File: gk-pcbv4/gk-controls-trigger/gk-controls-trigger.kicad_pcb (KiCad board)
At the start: 2 copper layers, 60 x 38.2 mm, 7 parts, among them J1 Conn_01x03, J2 Conn_01x01, J3 Conn_01x01, J4 Conn_01x01, J5 Conn_01x01

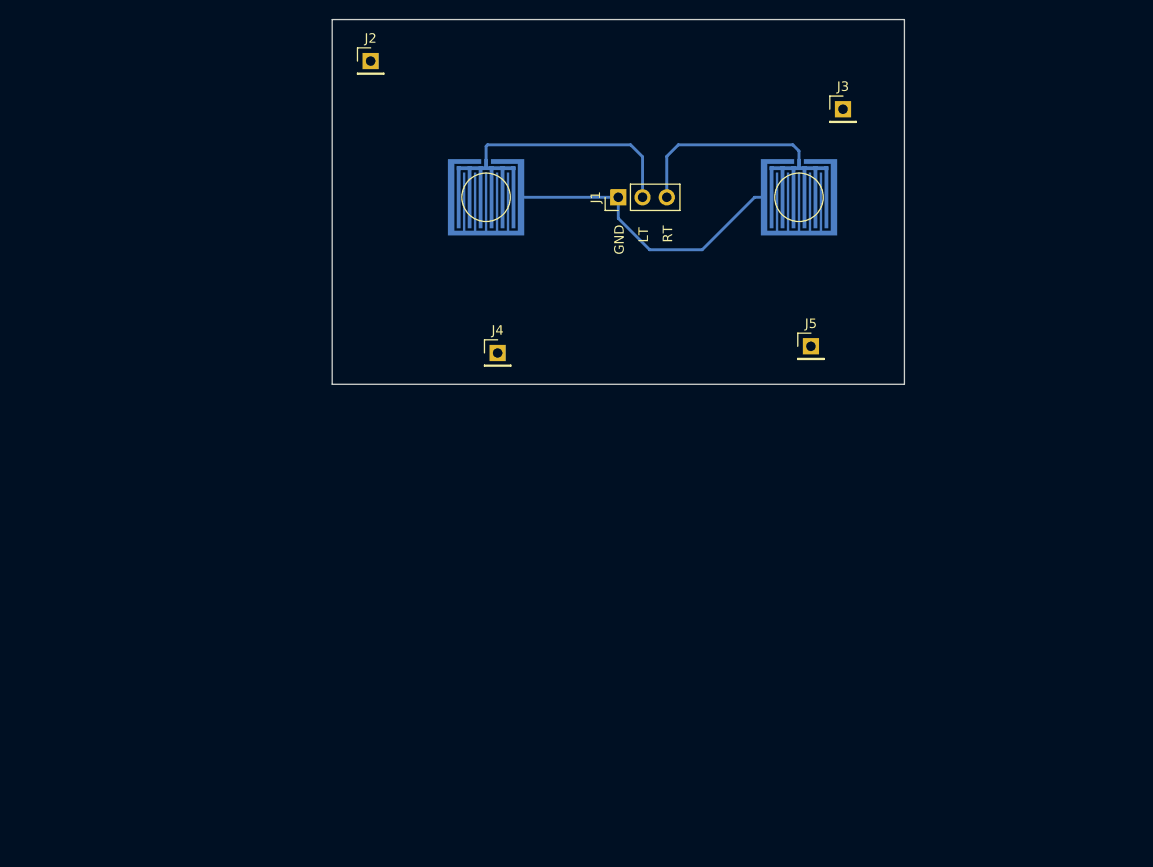
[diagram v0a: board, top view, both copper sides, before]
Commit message: update controls layout triggers now are analog new ADC on control board Move bumper buttons to trigger daughterboard and put in more ergonomical position
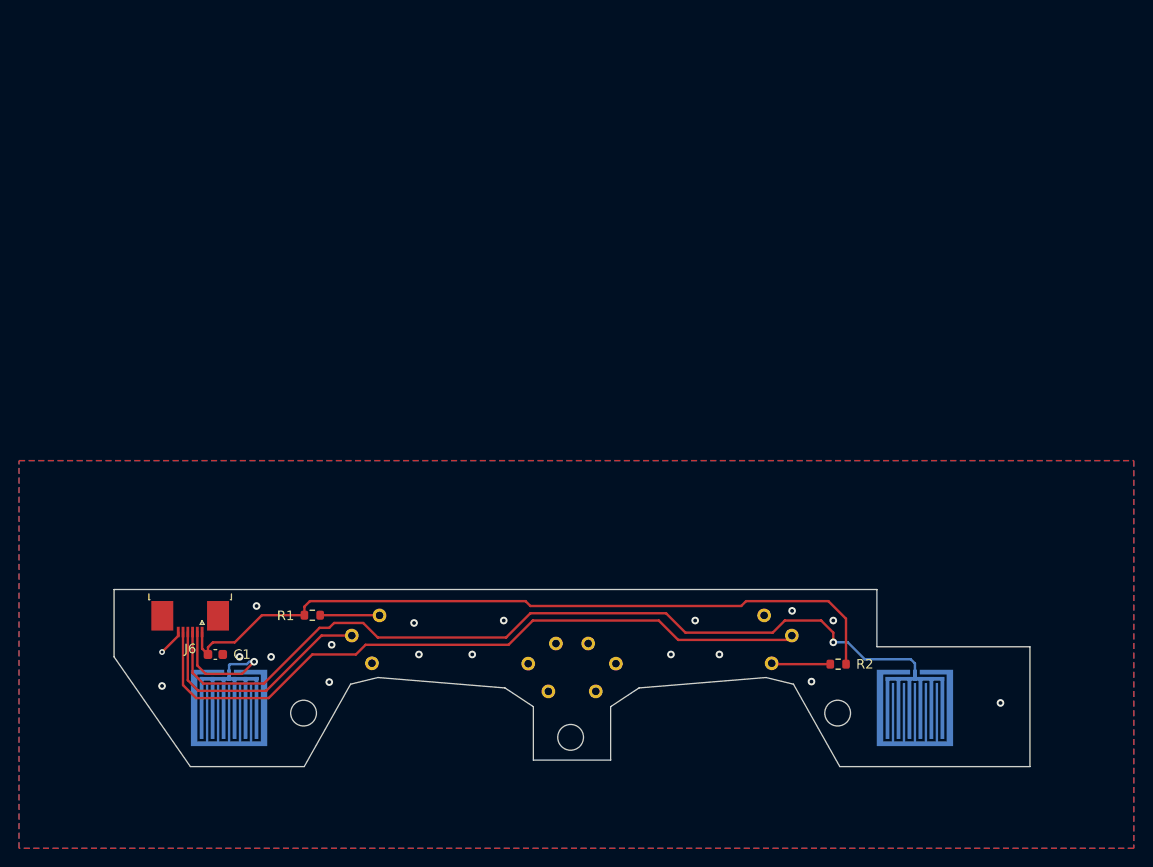
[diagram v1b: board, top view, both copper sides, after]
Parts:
- removed J1: Conn_01x03, Connector_PinHeader_2.54mm:PinHeader_1x03_P2.54mm_Vertical
- removed J2, J3, J4, J5: Conn_01x01, Connector_PinHeader_2.54mm:PinHeader_1x01_P2.54mm_Vertical
- added C1: 1u, Capacitor_SMD:C_0603_1608Metric, F.Cu at (46.0, 121.9)
- added H1: MountingHole, MountingHole:MountingHole_2.7mm_M2.5, F.Cu at (55.2, 128.1)
- added H2: MountingHole, MountingHole:MountingHole_2.7mm_M2.5, F.Cu at (83.2, 130.6)
- added H3: MountingHole, MountingHole:MountingHole_2.7mm_M2.5, F.Cu at (111.2, 128.1)
- added J6: Conn_01x06, Connector_FFC-FPC:TE_0-1734839-6_1x06-1MP_P0.5mm_Horizontal, F.Cu at (43.3, 118.2)
- added R1: 100k/0R, Resistor_SMD:R_0603_1608Metric, F.Cu at (56.1, 117.8)
- added R2: 100k/0R, Resistor_SMD:R_0603_1608Metric, F.Cu at (111.3, 122.9)
- added RV1: R_Potentiometer, Potentiometer_THT:Potentiometer_Bourns_3266W_Vertical, B.Cu at (63.2, 117.8)
- added RV2: R_Potentiometer, Potentiometer_THT:Potentiometer_Bourns_3266W_Vertical, B.Cu at (81.7, 120.8)
- added RV3: R_Potentiometer, Potentiometer_THT:Potentiometer_Bourns_3266W_Vertical, B.Cu at (85.8, 125.8)
- added RV4: R_Potentiometer, Potentiometer_THT:Potentiometer_Bourns_3266W_Vertical, B.Cu at (104.3, 122.8)
- moved SW_LB1 59.9 mm to (47.4, 127.5)
- moved SW_RB1 54.9 mm to (119.3, 127.5)
- renumbered SW_LT1 to SW_LB1, SW_RT1 to SW_RB1
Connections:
- net Net-(J1-Pin_1) renamed GND
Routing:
- net VDDA: track 0.00 -> 78.7 mm
- net RT_ANA: track 0.00 -> 74.3 mm
- net Net-(J6-Pin_3): track 20.3 -> 89.8 mm, vias 0 -> 1
- net GND: track 31.3 -> 2.80 mm, vias 0 -> 18
- net LT_ANA: track 0.00 -> 25.1 mm
- net Net-(J6-Pin_2): track 23.1 -> 14.2 mm, vias 0 -> 1
- net Net-(R1-Pad2): track 0.00 -> 6.23 mm
- net Net-(R2-Pad2): track 0.00 -> 6.18 mm
- added copper zone on B.Cu, net GND
- added copper zone on F.Cu, net GND
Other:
- board size 60 x 38.2 mm -> 96 x 18.6 mm
- board text removed: "GND"
- board text removed: "LT"
- board text removed: "RT"
